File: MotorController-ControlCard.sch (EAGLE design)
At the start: 45 parts, among them J2 SL03THROUGH_HOLE, Q7 MOSFET-PCHANNEL, Q8 MOSFET-PCHANNEL, U2 MAX3232D, U4 TMS320F28069MPZT

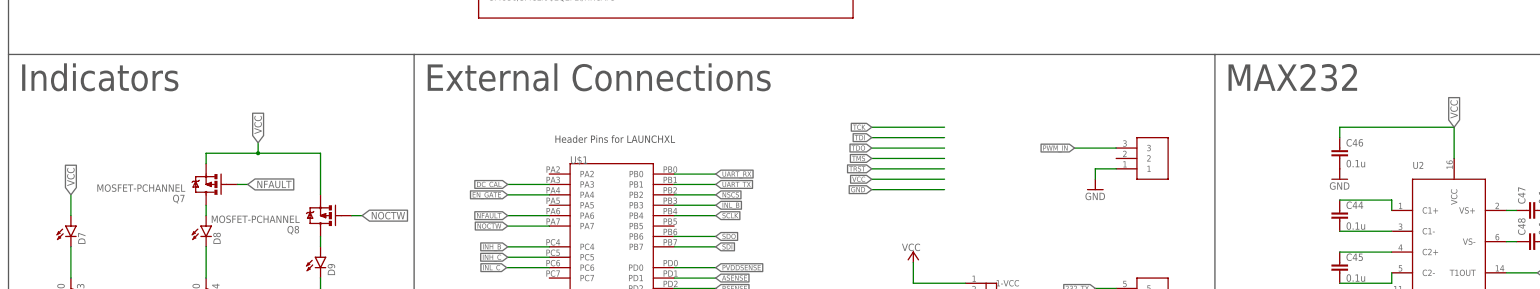
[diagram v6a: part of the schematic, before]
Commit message: Replaced incorrect VCC labels with actual VCC components. Removed leftover labels from schematic.
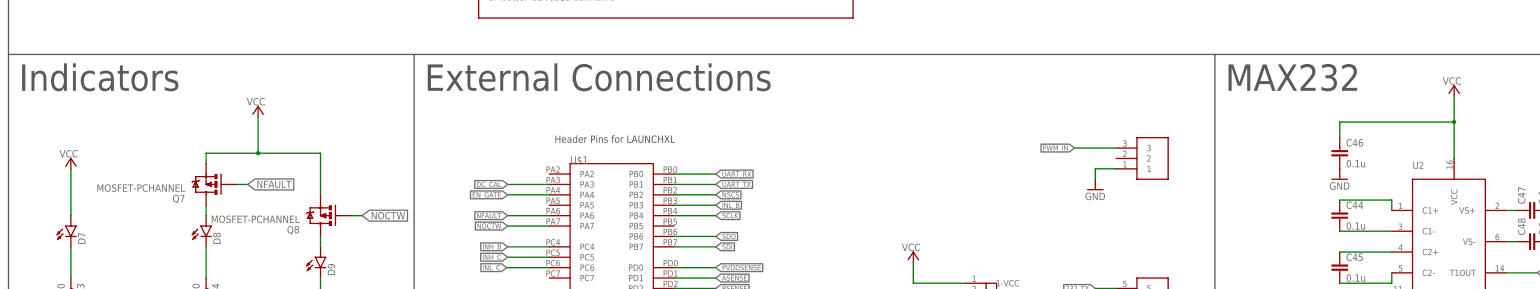
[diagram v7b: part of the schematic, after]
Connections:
- removed net VCC: C46.1, D7.A, Q7.S, Q8.S, U2.VCC
- net +3V3: now also C46.1, D7.A, Q7.S, Q8.S, U2.VCC
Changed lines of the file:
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@@
 <part name="U4" library="LAUNCHXL-F28027" deviceset="TMS320F28069PZS" device="R" value="TMS320F28069MPZT"/>
 <part name="GND5" library="supply1" library_urn="urn:adsk.eagle:library:371" deviceset="GND" device=""/>
+<part name="VCC3" library="supply1" library_urn="urn:adsk.eagle:library:371" deviceset="+3V3" device="" value="VCC"/>
+<part name="VCC4" library="supply1" library_urn="urn:adsk.eagle:library:371" deviceset="+3V3" device="" value="VCC"/>
+<part name="VCC5" library="supply1" library_urn="urn:adsk.eagle:library:371" deviceset="+3V3" device="" value="VCC"/>
 </parts>
 <sheets>
@@
 <instance part="U4" gate="G$3" x="-35.56" y="121.92"/>
 <instance part="GND5" gate="1" x="83.82" y="-96.52" rot="R270"/>
+<instance part="VCC3" gate="G$1" x="226.06" y="-33.02" smashed="yes">
+<attribute name="VALUE" x="223.266" y="-32.766" size="1.778" layer="96"/>
+</instance>
+<instance part="VCC4" gate="G$1" x="-66.04" y="-38.1" smashed="yes">
+<attribute name="VALUE" x="-68.834" y="-37.846" size="1.778" layer="96"/>
+</instance>
+<instance part="VCC5" gate="G$1" x="-111.76" y="-50.8" smashed="yes">
+<attribute name="VALUE" x="-114.554" y="-50.546" size="1.778" layer="96"/>
+</instance>
 </instances>
 <busses>
@@
 </segment>
 <segment>
-<wire x1="101.6" y1="-58.42" x2="83.82" y2="-58.42" width="0.1524" layer="91"/>
-<label x="83.82" y="-58.42" size="1.27" layer="95" rot="R180" xref="yes"/>
-</segment>
-<segment>
 <pinref part="R12" gate="G$1" pin="1"/>
 <pinref part="GND18" gate="1" pin="GND"/>
@@
 <wire x1="5.08" y1="-64.77" x2="-5.08" y2="-64.77" width="0.1524" layer="91"/>
 <label x="-5.08" y="-64.77" size="1.27" layer="95" rot="R180" xref="yes"/>
-</segment>
-</net>
-<net name="VCC" class="0">
-<segment>
-<pinref part="Q7" gate="G$1" pin="S"/>
-<wire x1="-78.74" y1="-52.07" x2="-78.74" y2="-49.53" width="0.1524" layer="91"/>
-<pinref part="Q8" gate="G$1" pin="S"/>
-<wire x1="-78.74" y1="-49.53" x2="-66.04" y2="-49.53" width="0.1524" layer="91"/>
-<wire x1="-66.04" y1="-49.53" x2="-50.8" y2="-49.53" width="0.1524" layer="91"/>
-<wire x1="-50.8" y1="-49.53" x2="-50.8" y2="-59.69" width="0.1524" layer="91"/>
-<wire x1="-66.04" y1="-49.53" x2="-66.04" y2="-46.99" width="0.1524" layer="91"/>
-<junction x="-66.04" y="-49.53"/>
-<label x="-66.04" y="-46.99" size="1.778" layer="95" rot="R90" xref="yes"/>
-</segment>
-<segment>
-<pinref part="D7" gate="G$1" pin="A"/>
-<wire x1="-111.76" y1="-64.77" x2="-111.76" y2="-59.69" width="0.1524" layer="91"/>
-<label x="-111.76" y="-59.69" size="1.778" layer="95" rot="R90" xref="yes"/>
-</segment>
-<segment>
-<wire x1="101.6" y1="-55.88" x2="83.82" y2="-55.88" width="0.1524" layer="91"/>
-<label x="83.82" y="-55.88" size="1.27" layer="95" rot="R180" xref="yes"/>
-</segment>
-<segment>
-<pinref part="U2" gate="G$1" pin="VCC"/>
-<wire x1="226.06" y1="-50.8" x2="226.06" y2="-43.18" width="0.1524" layer="91"/>
-<wire x1="226.06" y1="-43.18" x2="198.12" y2="-43.18" width="0.1524" layer="91"/>
-<pinref part="C46" gate="G$1" pin="1"/>
-<wire x1="198.12" y1="-43.18" x2="198.12" y2="-45.72" width="0.1524" layer="91"/>
-<label x="226.06" y="-43.18" size="1.778" layer="95" rot="R90" xref="yes"/>
 </segment>
 </net>
@@
 <wire x1="93.98" y1="-81.28" x2="106.68" y2="-81.28" width="0.1524" layer="91"/>
 </segment>
+<segment>
+<pinref part="VCC3" gate="G$1" pin="+3V3"/>
+<wire x1="226.06" y1="-35.56" x2="226.06" y2="-41.91" width="0.1524" layer="91"/>
+<pinref part="U2" gate="G$1" pin="VCC"/>
+<wire x1="226.06" y1="-50.8" x2="226.06" y2="-41.91" width="0.1524" layer="91"/>
+<wire x1="226.06" y1="-41.91" x2="198.12" y2="-41.91" width="0.1524" layer="91"/>
+<pinref part="C46" gate="G$1" pin="1"/>
+<wire x1="198.12" y1="-41.91" x2="198.12" y2="-45.72" width="0.1524" layer="91"/>
+<junction x="226.06" y="-41.91"/>
+</segment>
+<segment>
+<pinref part="VCC4" gate="G$1" pin="+3V3"/>
+<wire x1="-66.04" y1="-40.64" x2="-66.04" y2="-49.53" width="0.1524" layer="91"/>
+<pinref part="Q7" gate="G$1" pin="S"/>
+<wire x1="-78.74" y1="-52.07" x2="-78.74" y2="-49.53" width="0.1524" layer="91"/>
+<pinref part="Q8" gate="G$1" pin="S"/>
+<wire x1="-78.74" y1="-49.53" x2="-66.04" y2="-49.53" width="0.1524" layer="91"/>
+<wire x1="-66.04" y1="-49.53" x2="-50.8" y2="-49.53" width="0.1524" layer="91"/>
+<wire x1="-50.8" y1="-49.53" x2="-50.8" y2="-59.69" width="0.1524" layer="91"/>
+<junction x="-66.04" y="-49.53"/>
+</segment>
+<segment>
+<pinref part="VCC5" gate="G$1" pin="+3V3"/>
+<pinref part="D7" gate="G$1" pin="A"/>
+<wire x1="-111.76" y1="-64.77" x2="-111.76" y2="-53.34" width="0.1524" layer="91"/>
+</segment>
 </net>
 <net name="TCK" class="0">
@@
 </segment>
 <segment>
-<wire x1="101.6" y1="-43.18" x2="83.82" y2="-43.18" width="0.1524" layer="91"/>
-<label x="83.82" y="-43.18" size="1.27" layer="95" rot="R180" xref="yes"/>
-</segment>
-<segment>
 <pinref part="U$2" gate="1" pin="4-TCK"/>
 <wire x1="106.68" y1="-88.9" x2="96.52" y2="-88.9" width="0.1524" layer="91"/>
@@
 </segment>
 <segment>
-<wire x1="101.6" y1="-45.72" x2="83.82" y2="-45.72" width="0.1524" layer="91"/>
-<label x="83.82" y="-45.72" size="1.27" layer="95" rot="R180" xref="yes"/>
-</segment>
-<segment>
 <pinref part="U$2" gate="1" pin="8-TDI"/>
 <wire x1="106.68" y1="-99.06" x2="96.52" y2="-99.06" width="0.1524" layer="91"/>
@@
 </net>
 <net name="TDO" class="0">
-<segment>
-<wire x1="101.6" y1="-48.26" x2="83.82" y2="-48.26" width="0.1524" layer="91"/>
-<label x="83.82" y="-48.26" size="1.27" layer="95" rot="R180" xref="yes"/>
-</segment>
 <segment>
 <pinref part="R14" gate="G$1" pin="2"/>
@@
 </segment>
 <segment>
-<wire x1="101.6" y1="-50.8" x2="83.82" y2="-50.8" width="0.1524" layer="91"/>
-<label x="83.82" y="-50.8" size="1.27" layer="95" rot="R180" xref="yes"/>
-</segment>
-<segment>
 <pinref part="U$2" gate="1" pin="2-TMS"/>
 <wire x1="106.68" y1="-83.82" x2="96.52" y2="-83.82" width="0.1524" layer="91"/>
@@
 <net name="TRST" class="0">
 <segment>
-<wire x1="101.6" y1="-53.34" x2="83.82" y2="-53.34" width="0.1524" layer="91"/>
-<label x="83.82" y="-53.34" size="1.27" layer="95" rot="R180" xref="yes"/>
-</segment>
-<segment>
 <pinref part="R17" gate="G$1" pin="2"/>

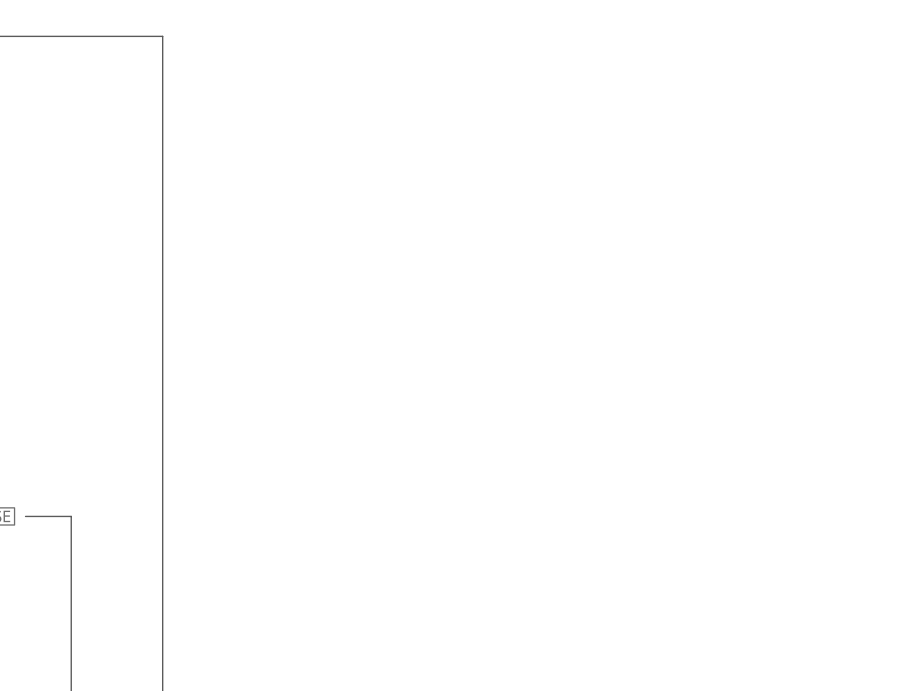
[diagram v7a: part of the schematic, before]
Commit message: BOM is now text file, and signatures have been added.
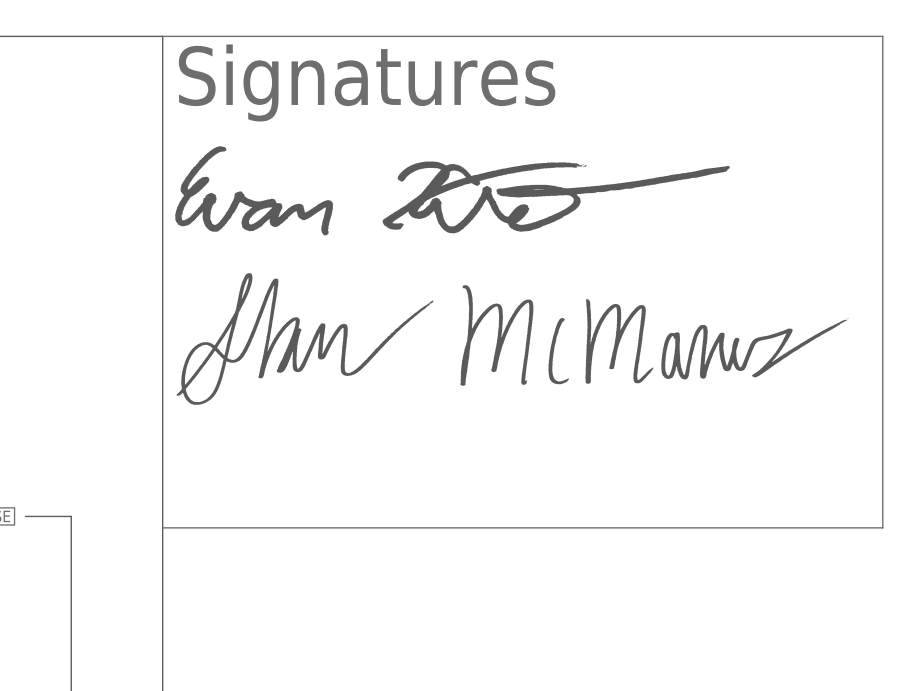
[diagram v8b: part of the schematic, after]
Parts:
- added U$3: EVAN_HITE_SIGNATURE, MRDT-Signatures:EVAN_HITE_SIGNATURE
- added U$5: SHAUN_MCMANUS_SIGNATURE, MRDT-Signatures:SHAUN_MCMANUS_SIGNATURE
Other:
- note added: "Signatures"
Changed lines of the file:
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@@
 <part name="VCC4" library="supply1" library_urn="urn:adsk.eagle:library:371" deviceset="+3V3" device="" value="VCC"/>
 <part name="VCC5" library="supply1" library_urn="urn:adsk.eagle:library:371" deviceset="+3V3" device="" value="VCC"/>
+<part name="U$3" library="MRDT-Signatures" deviceset="EVAN_HITE_SIGNATURE" device=""/>
+<part name="U$5" library="MRDT-Signatures" deviceset="SHAUN_MCMANUS_SIGNATURE" device=""/>
 </parts>
 <sheets>
@@
 <text x="170.18" y="-34.29" size="6.4516" layer="97">MAX232</text>
 <text x="6.35" y="-46.99" size="1.778" layer="97">Header Pins for LAUNCHXL</text>
+<wire x1="284.48" y1="193.04" x2="364.49" y2="193.04" width="0.1524" layer="95"/>
+<wire x1="364.49" y1="193.04" x2="364.49" y2="138.43" width="0.1524" layer="95"/>
+<wire x1="364.49" y1="138.43" x2="284.48" y2="138.43" width="0.1524" layer="95"/>
+<text x="285.75" y="185.42" size="6.4516" layer="95" font="vector">Signatures</text>
 </plain>
 <instances>
@@
 <attribute name="VALUE" x="-114.554" y="-50.546" size="1.778" layer="96"/>
 </instance>
+<instance part="U$3" gate="G$1" x="285.75" y="168.91"/>
+<instance part="U$5" gate="G$1" x="285.75" y="152.4"/>
 </instances>
 <busses>
